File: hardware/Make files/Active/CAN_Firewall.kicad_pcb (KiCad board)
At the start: 2 copper layers, 68 x 44 mm, 60 parts, among them CON1 BARREL_JACK, CON2 AVR-JTAG-10, CON3 AVR-AW-6, J1 +5V_SRC, J2 DB9, J3 DB9, P1 USB_OTG, P2 USB_OTG, P3 DIAG Port, SW1 SPST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

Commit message: V1.11
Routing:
- net GND: track 303.8 -> 333.1 mm, vias 59 -> 65

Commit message: V1.11 Proofed
Ready to order
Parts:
- added D3: SMBJ16A, Diodes_SMD:SMB_Standard, F.Cu at (50.8, 122.5)
- added R20: 120, Custom Parts:R_0603_sm, F.Cu at (48.5, 130.0)
- added R21: 120, Custom Parts:R_0603_sm, F.Cu at (105.0, 132.5)
- added REF**: MountingHole_3-5mm, Mounting_Holes:MountingHole_3-5mm, F.Cu at (95.5, 159.0)
- added REF**: MountingHole_3-5mm, Mounting_Holes:MountingHole_3-5mm, F.Cu at (50.5, 159.1)
- added REF**: MountingHole_3-5mm, Mounting_Holes:MountingHole_3-5mm, F.Cu at (50.5, 109.0)
- added REF**: Symbol_OSHW-Logo_SilkScreen_BIG, Symbols:Symbol_OSHW-Logo_SilkScreen_BIG, B.Cu at (95.3, 101.0)
- added REF**: MountingHole_3-5mm, Mounting_Holes:MountingHole_3-5mm, F.Cu at (95.5, 109.0)
- added SW2: SPST, Custom Parts:SW_SPST_FSMSM_SM, F.Cu at (53.0, 133.5)
- added SW3: SPST, Custom Parts:SW_SPST_FSMSM_SM, F.Cu at (96.0, 132.5)
- moved R11 17.5 mm to (98.0, 117.5)
- moved F2 17.4 mm to (105.0, 128.5), turned to 90 degrees
- moved R10 17.4 mm to (93.5, 117.5), turned to 0 degrees
- moved D1 15.9 mm to (93.5, 114.5), turned to 180 degrees
- moved FB2 14.9 mm to (79.9, 125.1), turned to 0 degrees
- moved C2 8.90 mm to (105.0, 124.5)
- moved D2 8.90 mm to (98.0, 114.5)
- moved C11 8.14 mm to (87.5, 127.0)
- moved C1 7.75 mm to (50.0, 114.0), turned to 0 degrees
- moved P1 7.38 mm to (40.5, 115.0), turned to 270 degrees
- moved P2 7.38 mm to (107.5, 115.0), turned to 90 degrees
- moved R8 7.16 mm to (80.0, 122.5)
- moved C3 7.02 mm to (105.0, 122.0), turned to 0 degrees
- moved R9 6.96 mm to (85.0, 122.5)
- moved U4 6.10 mm to (98.0, 148.5), turned to 270 degrees
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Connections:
- U1 pad 58: (no net) -> LED1
- U1 pad 59: (no net) -> LED2
- U1 pad 62: LED1 -> (no net)
- U1 pad 63: LED2 -> (no net)
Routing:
- net Net-(F2-Pad1): track 3.71 -> 27.2 mm
- net USB5: track 43.9 -> 23.2 mm
- net +5V: track 233.2 -> 218.7 mm
- net Net-(R8-Pad1): track 16.7 -> 30.8 mm, vias 0 -> 2
- net Net-(C2-Pad1): track 14.1 -> 0.00 mm, vias 2 -> 0
- net CAR_CANH: track 16.4 -> 28.7 mm, vias 0 -> 2
- net CAR_CANL: track 18.0 -> 29.5 mm
- net Net-(D2-Pad2): track 14.4 -> 3.02 mm
- net IVI_CANL: track 14.0 -> 25.4 mm, vias 0 -> 2
- net IVI_CANH: track 11.1 -> 22.2 mm, vias 1 -> 3
- net ~RESET/A_DATA: track 103.0 -> 112.7 mm
- net Net-(C1-Pad1): track 11.2 -> 2.08 mm, vias 2 -> 0
- net +12V: track 111.7 -> 103.5 mm, vias 4 -> 3
- net Net-(D2-Pad1): track 14.9 -> 7.26 mm, vias 2 -> 0
- net Net-(D1-Pad1): track 13.7 -> 7.35 mm, vias 2 -> 0
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- added copper zone on F.Cu, net +5V
- added copper zone on F.Cu, net Net-(C1-Pad1)
- added copper zone on F.Cu, net Net-(C2-Pad1)
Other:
- board size 68 x 44 mm -> 68 x 58 mm
- board text added: "120 ohm Terminator"
- board text added: "A/B LOOP JUMPER"
- board text added: "BOOT USB REG. +12V DEBUG USB"
- board text added: "CAR CAN"
- board text added: "GND"
- board text added: "Jaguar Land Rovver CANBUS Firewall V1.11 Open Source Hardware Jesse Banks 2015"
- board text added: "LED1"
- board text added: "LED2"
- board text added: "Power "ON" LED"
- board text removed: "BOOT USB +12V DEBUG USB"
- board text removed: "Jaguar Land Rovver CANBUS Firewall V1.1 Open Source Hardware Jesse Banks 2015"
- board text removed: "LOOP JUMPER"
- board text removed: "PWR"

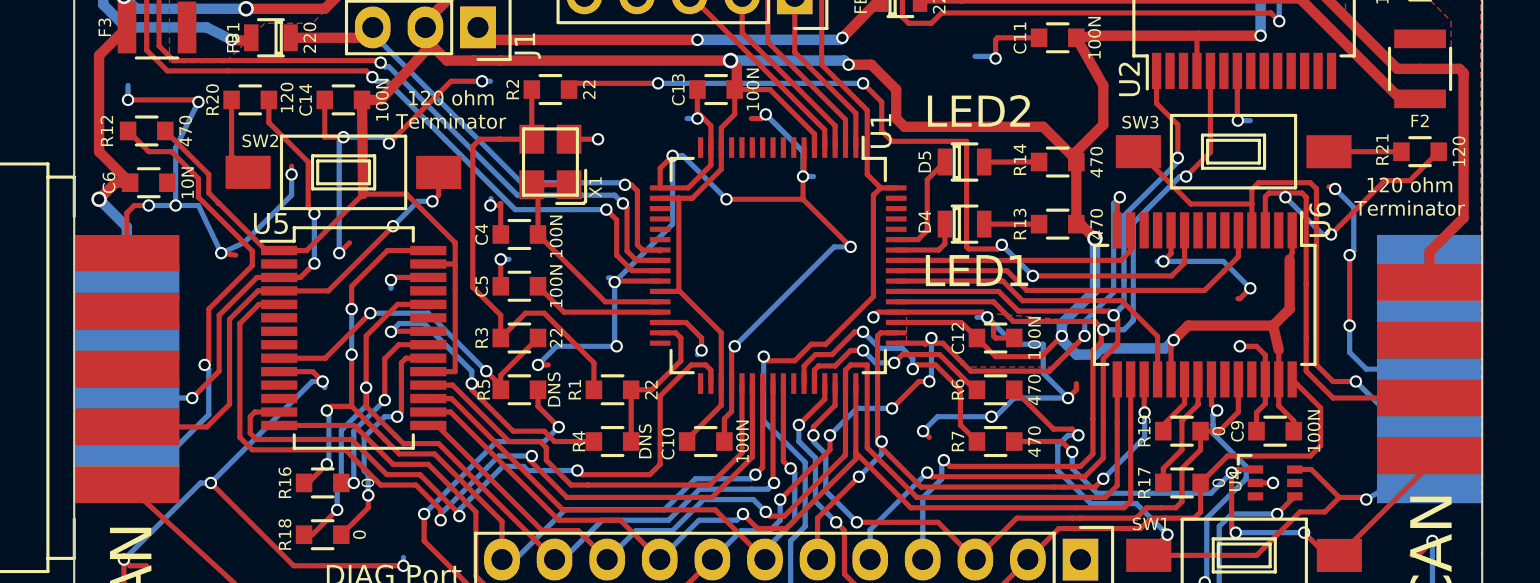
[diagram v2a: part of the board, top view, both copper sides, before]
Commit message: Fixed CanH-CanL swap
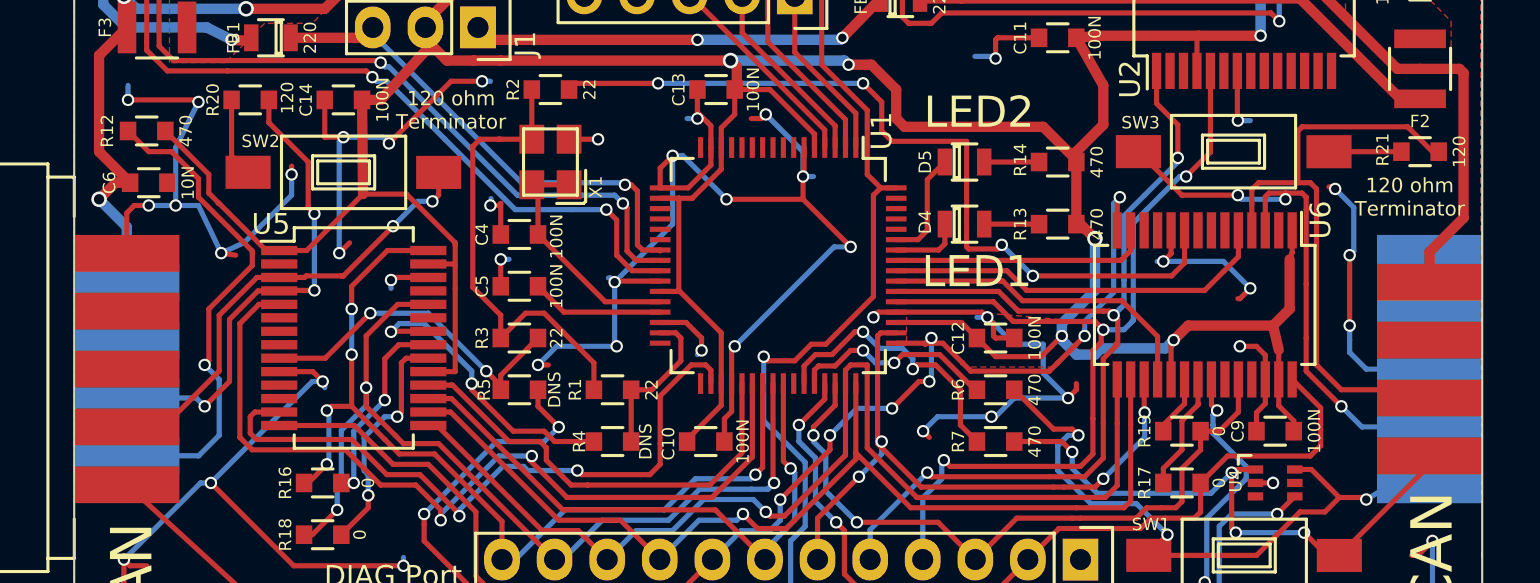
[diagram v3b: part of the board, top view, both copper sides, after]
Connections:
- CON1 pad 3: (no net) -> Net-(CON1-Pad3)
- CON2 pad 7: (no net) -> Net-(CON2-Pad7)
- CON2 pad 8: (no net) -> Net-(CON2-Pad8)
- CON3 pad 3: (no net) -> Net-(CON3-Pad3)
- CON3 pad 4: (no net) -> Net-(CON3-Pad4)
- CON3 pad 5: (no net) -> Net-(CON3-Pad5)
- J2 pad 4: (no net) -> Net-(J2-Pad4)
- J2 pad 8: (no net) -> Net-(J2-Pad8)
- J3 pad 4: (no net) -> Net-(J3-Pad4)
- J3 pad 8: (no net) -> Net-(J3-Pad8)
- P1 pad 4: (no net) -> Net-(P1-Pad4)
- P2 pad 4: (no net) -> Net-(P2-Pad4)
- U1 pad 10: (no net) -> Net-(U1-Pad10)
- U1 pad 11: (no net) -> Net-(U1-Pad11)
- U1 pad 12: (no net) -> Net-(U1-Pad12)
- U1 pad 13: (no net) -> Net-(U1-Pad13)
- U1 pad 16: (no net) -> Net-(U1-Pad16)
- U1 pad 19: (no net) -> Net-(U1-Pad19)
- U1 pad 20: (no net) -> Net-(U1-Pad20)
- U1 pad 21: (no net) -> Net-(U1-Pad21)
- U1 pad 22: (no net) -> Net-(U1-Pad22)
- U1 pad 32: (no net) -> Net-(U1-Pad32)
- U1 pad 33: (no net) -> Net-(U1-Pad33)
- U1 pad 42: (no net) -> Net-(U1-Pad42)
- U1 pad 60: (no net) -> Net-(U1-Pad60)
- U1 pad 61: (no net) -> Net-(U1-Pad61)
- U1 pad 62: (no net) -> Net-(U1-Pad62)
- U1 pad 63: (no net) -> Net-(U1-Pad63)
- U1 pad 7: (no net) -> Net-(U1-Pad7)
- U1 pad 8: (no net) -> Net-(U1-Pad8)
- U1 pad 9: (no net) -> Net-(U1-Pad9)
- U2 pad 10: (no net) -> Net-(U2-Pad10)
- U2 pad 11: (no net) -> Net-(U2-Pad11)
- U2 pad 12: (no net) -> Net-(U2-Pad12)
- U2 pad 13: (no net) -> Net-(U2-Pad13)
- U2 pad 14: (no net) -> Net-(U2-Pad14)
- U2 pad 2: (no net) -> Net-(U2-Pad2)
- U2 pad 27: (no net) -> Net-(U2-Pad27)
- U2 pad 28: (no net) -> Net-(U2-Pad28)
- U2 pad 3: (no net) -> Net-(U2-Pad3)
- U2 pad 6: (no net) -> Net-(U2-Pad6)
- U2 pad 9: (no net) -> Net-(U2-Pad9)
- U4 pad 3: (no net) -> Net-(U4-Pad3)
- U4 pad 5: (no net) -> Net-(U4-Pad5)
- U5 pad 11: (no net) -> IVI_Rx1BF
- U5 pad 12: (no net) -> IVI_Rx0BF
- U5 pad 2: (no net) -> Net-(U5-Pad2)
- U5 pad 23: (no net) -> IVI_Tx0RTS
- U5 pad 25: (no net) -> Net-(U5-Pad25)
- U5 pad 3: IVI_CANH -> IVI_CANL
- U5 pad 4: IVI_CANL -> IVI_CANH
- U5 pad 6: (no net) -> IVI_Tx1RTS
- U5 pad 7: (no net) -> IVI_Tx2RTS
- U5 pad 8: (no net) -> Net-(U5-Pad8)
- U6 pad 11: (no net) -> CAR_Rx1BF
- U6 pad 12: (no net) -> CAR_Rx0BF
- U6 pad 2: (no net) -> Net-(U6-Pad2)
- U6 pad 23: (no net) -> CAR_Tx0RTS
- U6 pad 25: (no net) -> Net-(U6-Pad25)
- U6 pad 3: CAR_CANH -> CAR_CANL
- U6 pad 4: CAR_CANL -> CAR_CANH
- U6 pad 6: (no net) -> CAR_Tx1RTS
- U6 pad 7: (no net) -> CAR_Tx2RTS
- U6 pad 8: (no net) -> Net-(U6-Pad8)
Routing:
- net Net-(J2-Pad6): track 24.1 -> 27.4 mm
- net CAR_CANL: track 29.5 -> 31.4 mm, vias 1 -> 3
- net IVI_CANH: track 22.2 -> 23.4 mm
- net CAR_CANH: track 28.7 -> 29.9 mm, vias 2 -> 0
- net IVI_CANL: track 25.4 -> 24.6 mm

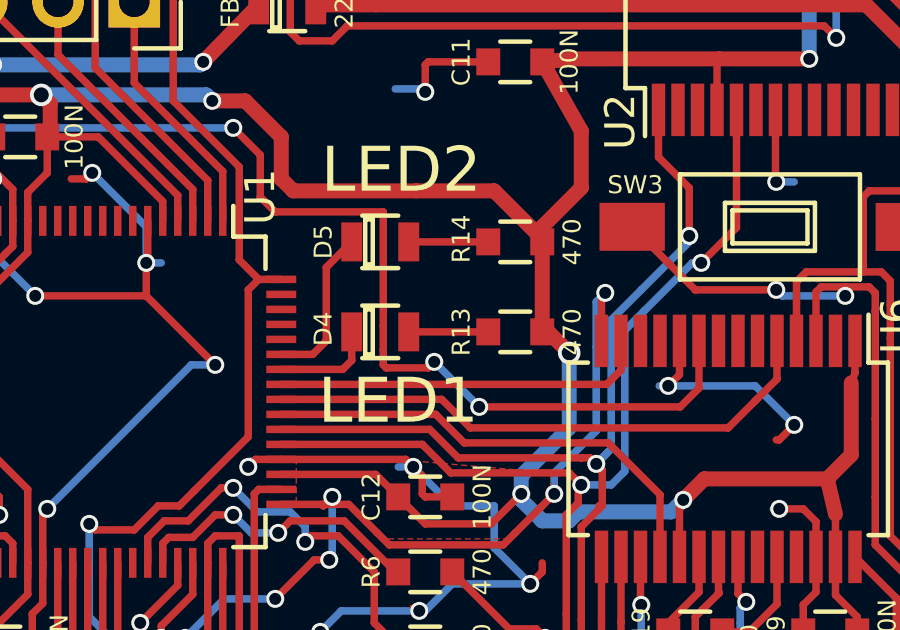
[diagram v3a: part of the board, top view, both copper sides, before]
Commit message: Moved CAR Interupt signal to different Pin
Steve needed the car side can controller interupt signal to go to a
different pin because of some inherent traits of the original pin
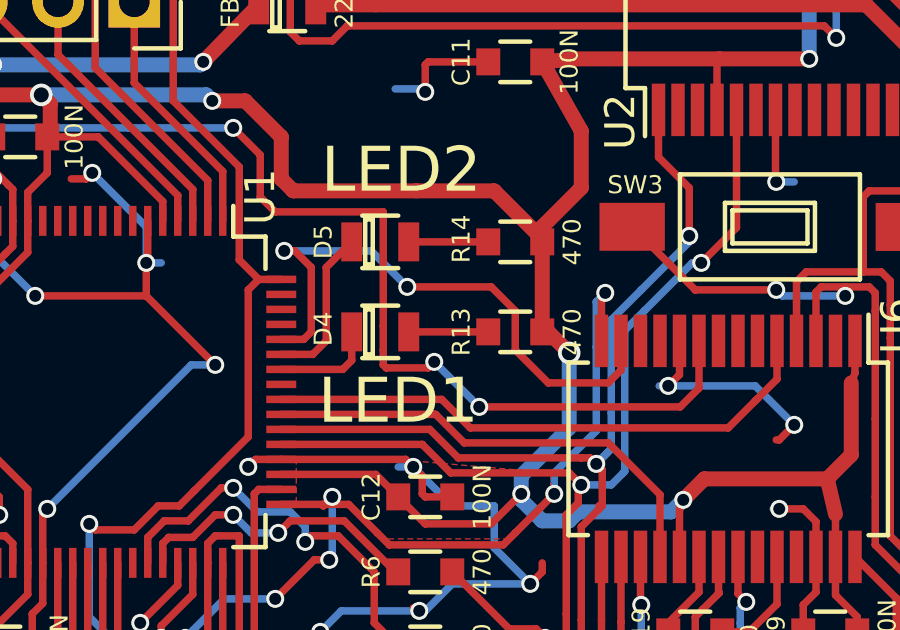
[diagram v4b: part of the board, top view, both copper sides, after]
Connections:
- U1 pad 57: CAR_INT -> Net-(U1-Pad57)
- U1 pad 60: Net-(U1-Pad60) -> CAR_INT
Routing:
- net CAR_INT: track 12.5 -> 19.3 mm, vias 0 -> 2

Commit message: progress towards V1.2
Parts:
- added JP1: Matrix A, Connect:GS3, F.Cu at (53.6, 173.5)
- added JP10: Matrix E, Connect:GS3, F.Cu at (82.2, 174.2)
- added JP2: Matrix B, Connect:GS3, F.Cu at (49.3, 173.1)
- added JP3: Matrix C, Connect:GS3, F.Cu at (45.7, 173.3)
- added JP4: Matrix D, Connect:GS3, F.Cu at (58.2, 173.4)
- added JP5: Matrix E, Connect:GS3, F.Cu at (77.9, 173.8)
- added JP6: Matrix A, Connect:GS3, F.Cu at (65.2, 174.1)
- added JP7: Matrix B, Connect:GS3, F.Cu at (91.9, 174.0)
- added JP8: Matrix C, Connect:GS3, F.Cu at (97.9, 174.0)
- added JP9: Matrix D, Connect:GS3, F.Cu at (85.6, 174.2)
- C7: value 4U7 -> 47U
- CON2, CON3: moved to B.Cu
- D1: value RED -> YELLOW
- D2: value BLUE -> WHITE
- D5: value BLUE -> GREEN
- R4, R5: value DNS -> 470
- moved R12 64.9 mm to (73.5, 189.0)
- moved C14 34.9 mm to (87.5, 124.5)
- moved C11 34.6 mm to (53.0, 130.0)
- moved R5 31.1 mm to (87.5, 127.0)
- moved R4 27.4 mm to (87.5, 129.5), turned to 0 degrees
- moved R16 17.0 mm to (35.0, 149.2)
- moved R18 16.9 mm to (35.1, 151.4)
- moved CON2 9.81 mm to (65.0, 125.5), turned to 0 degrees
- moved X1 8.54 mm to (60.0, 141.0), turned to 180 degrees
- moved C5 8.14 mm to (60.0, 147.0)
- moved R3 7.16 mm to (60.0, 134.5), turned to 0 degrees
- moved R1 6.02 mm to (60.0, 144.5)
- moved R8 5.41 mm to (83.0, 127.0)
- moved FB2 5.38 mm to (83.0, 129.5)
- moved D6 5.30 mm to (75.5, 108.7)
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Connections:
- C14 pad 1: +5V -> USB5
- J2 pad 1: ~RESET/A_DATA -> Net-(J2-Pad1)
- J2 pad 5: GND -> Net-(J2-Pad5)
- J3 pad 1: LOOP_B -> A
- J3 pad 4: Net-(J3-Pad4) -> B
- J3 pad 5: GND -> C
- J3 pad 6: LOOP_A -> D
- J3 pad 8: Net-(J3-Pad8) -> E
- R10 pad 2: +5V -> USB5
- R11 pad 2: +5V -> USB5
- R12 pad 1: Net-(J2-Pad6) -> Net-(JP10-Pad1)
- R4 pad 1: CLK1 -> RX_DBG
- R4 pad 2: CLK3_OUT -> Net-(R4-Pad2)
- R5 pad 1: CLK3 -> TX_DBG
- R5 pad 2: CLK2_OUT -> Net-(R5-Pad2)
- U2 pad 1: RX_DBG -> Net-(R4-Pad2)
- U2 pad 20: +5V -> USB5
- U2 pad 4: +5V -> USB5
- U2 pad 5: TX_DBG -> Net-(R5-Pad2)
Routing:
- net GND: track 328.0 -> 166.4 mm, vias 61 -> 39
- net (no net): track 0.00 -> 82.2 mm, vias 0 -> 6
- net ~RESET/A_DATA: track 112.7 -> 30.8 mm, vias 4 -> 0
- net CLK2_OUT: track 62.5 -> 0.00 mm, vias 4 -> 0
- net +5V: track 218.7 -> 171.8 mm, vias 7 -> 5
- net USB5: track 23.2 -> 68.5 mm
- net Net-(J2-Pad6): track 27.4 -> 3.44 mm, vias 1 -> 0
- net CLK3: track 16.5 -> 0.00 mm, vias 2 -> 0
- net CLK3_OUT: track 14.7 -> 0.00 mm, vias 2 -> 0
- net Net-(R18-Pad2): track 11.6 -> 0.00 mm, vias 2 -> 0
- net +3V3: track 11.6 -> 0.00 mm
- net Net-(R5-Pad2): track 0.00 -> 10.4 mm, vias 0 -> 2
- net Net-(F1-Pad1): track 11.3 -> 1.10 mm, vias 2 -> 0
- net TDI: track 19.2 -> 9.04 mm
- net Net-(R16-Pad2): track 9.60 -> 0.00 mm, vias 2 -> 0
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- removed copper zone on F.Cu, net Net-(C1-Pad1)
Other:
- board text added: "LED1 RED"
- board text added: "LED2 GREEN"
- board text removed: "LED1"
- board text removed: "LED2"
